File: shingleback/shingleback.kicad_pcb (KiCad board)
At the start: 2 copper layers, 117.8 x 86.2 mm, 45 parts

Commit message: final rev1 commit before manufacturing
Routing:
- net (no net): track 829.0 -> 841.0 mm

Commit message: shingleback rev2
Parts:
- removed the ? at (125.0, 83.5)
- removed the ? at (162.2, 30.7)
- removed the ? at (118.5, 88.0)
- removed the ? at (125.0, 88.0)
- removed the ? at (155.8, 30.7)
- removed the ? at (118.5, 83.5)
- removed the ? at (155.8, 26.2)
- removed the ? at (162.2, 26.2)
- removed the R at (131.8, 105.0)
- removed the R at (150.8, 67.0)
- removed the R at (93.8, 48.0)
- removed the R at (164.5, 108.2)
- removed the R at (150.8, 105.0)
- removed the R at (129.2, 57.8)
- removed the R at (131.8, 48.0)
- removed the R at (148.2, 67.0)
- removed the R at (150.8, 48.0)
- removed the R at (110.2, 67.0)
- removed the R at (129.2, 76.8)
- removed the R at (91.2, 86.0)
- removed the R at (91.2, 105.0)
- removed the R at (112.8, 38.8)
- removed the R at (110.2, 86.0)
- removed the R at (148.2, 86.0)
- removed the REF at (185.0, 62.0)
- removed the REF at (185.0, 88.2)
- removed the REF** at (161.5, 73.8)
- removed the REF** at (183.7, 100.8)
- removed the REF** at (176.1, 94.9)
- removed the S14 at (159.0, 62.1)
- removed the S14 at (140.0, 62.1)
- removed the S14 at (121.0, 71.8)
- removed the S14 at (140.0, 81.1)
- removed the S14 at (102.0, 81.1)
- removed the S14 at (121.0, 52.8)
- removed the S14 at (140.0, 100.1)
- removed the S14 at (121.0, 33.8)
- removed the S14 at (102.0, 43.1)
- removed the S14 at (140.0, 43.1)
- removed the S14 at (159.1, 100.1)
- removed the S14 at (83.0, 81.1)
- removed the S14 at (102.0, 62.1)
- removed the S14 at (159.0, 43.1)
- removed the S14 at (83.0, 100.1)
- added ?: , , F.Cu at (76.0, 101.0)
- added ?: , , F.Cu at (76.0, 105.5)
- added ?: , , F.Cu at (36.5, 58.0)
- added ?: , , F.Cu at (43.0, 58.0)
- added ?: , , F.Cu at (60.5, 105.5)
- added ?: , , F.Cu at (30.0, 73.9)
- added ?: , , F.Cu at (30.0, 79.0)
- added ?: , , F.Cu at (30.0, 76.5)
- added ?: , , F.Cu at (69.5, 105.5)
- added ?: , , F.Cu at (36.5, 53.5)
- added ?: , , F.Cu at (43.0, 53.5)
- added ?: , , F.Cu at (67.0, 101.0)
- added ?: , , F.Cu at (60.5, 101.0)
- added ?: , , F.Cu at (30.0, 81.5)
- added ?: , , F.Cu at (78.5, 105.5)
- added ?: , , F.Cu at (69.5, 101.0)
- added ?: , , F.Cu at (85.0, 105.5)
- added ?: , , F.Cu at (30.0, 84.1)
- added ?: , , F.Cu at (78.5, 101.0)
- added ?: , , F.Cu at (67.0, 105.5)
- added ?: , , F.Cu at (85.0, 101.0)
- added R: d, Diode_THT:D_DO-35_SOD27_P7.62mm_Horizontal, F.Cu at (46.5, 93.6)
- added R: d, Diode_THT:D_DO-35_SOD27_P7.62mm_Horizontal, F.Cu at (46.5, 74.6)
- added R: d, Diode_THT:D_DO-35_SOD27_P7.62mm_Horizontal, F.Cu at (107.0, 111.1)
- added R: d, Diode_THT:D_DO-35_SOD27_P7.62mm_Horizontal, F.Cu at (39.5, 101.0)
- added R: d, Diode_THT:D_DO-35_SOD27_P7.62mm_Horizontal, F.Cu at (50.0, 55.6)
- added R: d, Diode_THT:D_DO-35_SOD27_P7.62mm_Horizontal, F.Cu at (69.0, 74.6)
- added R: d, Diode_THT:D_DO-35_SOD27_P7.62mm_Horizontal, F.Cu at (88.0, 111.1)
- added R: d, Diode_THT:D_DO-35_SOD27_P7.62mm_Horizontal, F.Cu at (50.0, 93.6)
- added R: d, Diode_THT:D_DO-35_SOD27_P7.62mm_Horizontal, F.Cu at (69.0, 55.6)
- added R: d, Diode_THT:D_DO-35_SOD27_P7.62mm_Horizontal, F.Cu at (107.0, 55.6)
- added R: d, Diode_THT:D_DO-35_SOD27_P7.62mm_Horizontal, F.Cu at (49.5, 101.0)
- added R: d, Diode_THT:D_DO-35_SOD27_P7.62mm_Horizontal, F.Cu at (125.5, 92.5)
- added R: d, Diode_THT:D_DO-35_SOD27_P7.62mm_Horizontal, F.Cu at (88.0, 74.6)
- added R: d, Diode_THT:D_DO-35_SOD27_P7.62mm_Horizontal, F.Cu at (49.9, 74.6)
- added R: d, Diode_THT:D_DO-35_SOD27_P7.62mm_Horizontal, F.Cu at (69.0, 93.6)
- added R: d, Diode_THT:D_DO-35_SOD27_P7.62mm_Horizontal, F.Cu at (126.0, 111.1)
- added R: d, Diode_THT:D_DO-35_SOD27_P7.62mm_Horizontal, F.Cu at (88.0, 93.6)
- added R: d, Diode_THT:D_DO-35_SOD27_P7.62mm_Horizontal, F.Cu at (44.5, 101.0)
- added R: d, Diode_THT:D_DO-35_SOD27_P7.62mm_Horizontal, F.Cu at (107.0, 74.6)
- added R: d, Diode_THT:D_DO-35_SOD27_P7.62mm_Horizontal, F.Cu at (88.0, 55.6)
- added REF: RJ45_gnawman, Connector_RJ:RJ45_gnawman, F.Cu at (140.0, 74.0)
- added REF: RJ45_gnawman, Connector_RJ:RJ45_gnawman, B.Cu at (140.0, 98.0)
- added REF**: RotaryEncoder_gnawman, Rotary_Encoder:RotaryEncoder_gnawman, F.Cu at (118.0, 81.2)
- added S14: , MX, F.Cu at (95.8, 107.5)
- added S14: , MX, F.Cu at (114.8, 50.5)
- added S14: , MX, F.Cu at (95.8, 69.5)
- added S14: , MX, F.Cu at (114.8, 107.5)
- added S14: , MX, F.Cu at (38.8, 88.5)
- added S14: , MX, F.Cu at (76.8, 88.5)
- added S14: , MX, F.Cu at (95.8, 50.5)
- added S14: , MX, F.Cu at (57.8, 88.5)
- added S14: , MX, F.Cu at (95.8, 88.5)
- added S14: , MX, F.Cu at (114.8, 69.5)
- added S14: , MX, F.Cu at (76.8, 50.5)
- added S14: , MX, F.Cu at (133.8, 107.5)
- added S14: , MX, F.Cu at (76.8, 69.5)
- added S14: , MX, F.Cu at (57.8, 50.5)
- added S14: , MX, F.Cu at (38.8, 69.5)
- added S14: , MX, F.Cu at (57.8, 69.5)
- moved MCU1 46.4 mm to (133.6, 59.0)
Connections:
- MCU1 pad 1: (no net) -> rot1
- MCU1 pad 10: col6 -> row3
- MCU1 pad 11: col7 -> row4
- MCU1 pad 12: col8 -> row5
- MCU1 pad 13: (no net) -> RAW
- MCU1 pad 14: GND -> (no net)
- MCU1 pad 15: (no net) -> RST
- MCU1 pad 17: (no net) -> col8
- MCU1 pad 18: (no net) -> col7
- MCU1 pad 19: (no net) -> col6
- MCU1 pad 2: (no net) -> rot2
- MCU1 pad 20: (no net) -> col5
- MCU1 pad 21: row1 -> col4
- MCU1 pad 22: row2 -> col3
- MCU1 pad 23: row3 -> col2
- MCU1 pad 24: row4 -> col1
- MCU1 pad 4: GND -> (no net)
- MCU1 pad 5: col1 -> row1
- MCU1 pad 6: col2 -> exp3
- MCU1 pad 7: col3 -> exp2
- MCU1 pad 8: col4 -> exp1
- MCU1 pad 9: col5 -> row2
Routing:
- net (no net): track 841.0 -> 306.1 mm
- net RST: track 0.00 -> 118.7 mm
- net exp1: track 0.00 -> 114.0 mm
- net col4: track 110.7 -> 224.5 mm
- net exp2: track 0.00 -> 110.9 mm
- net exp3: track 0.00 -> 109.9 mm
- net row5: track 0.00 -> 105.8 mm
- net col1: track 246.3 -> 160.9 mm
- net VCC: track 79.5 -> 146.3 mm
- net row1: track 180.5 -> 117.8 mm, vias 1 -> 0
- net row2: track 177.7 -> 120.7 mm, vias 1 -> 0
- net col3: track 165.6 -> 222.4 mm
- net row4: track 139.9 -> 95.8 mm
- net rot1: track 0.00 -> 41.6 mm
- net rot2: track 0.00 -> 37.0 mm
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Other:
- board size 117.8 x 86.2 mm -> 119.5 x 76 mm
- board text added: "EX1"
- board text added: "EX2"
- board text added: "EX3"
- board text added: "GND"
- board text added: "VCC"
- board text added: "shingleback rev2"
- board text removed: "button"
- board text removed: "empty"
- board text removed: "joy"
- board text removed: "rj45"
- board text removed: "shingleback rev1"
- board text removed: "stick"
- board text removed: "switch"
- board text removed: "this space intentionally left blank"

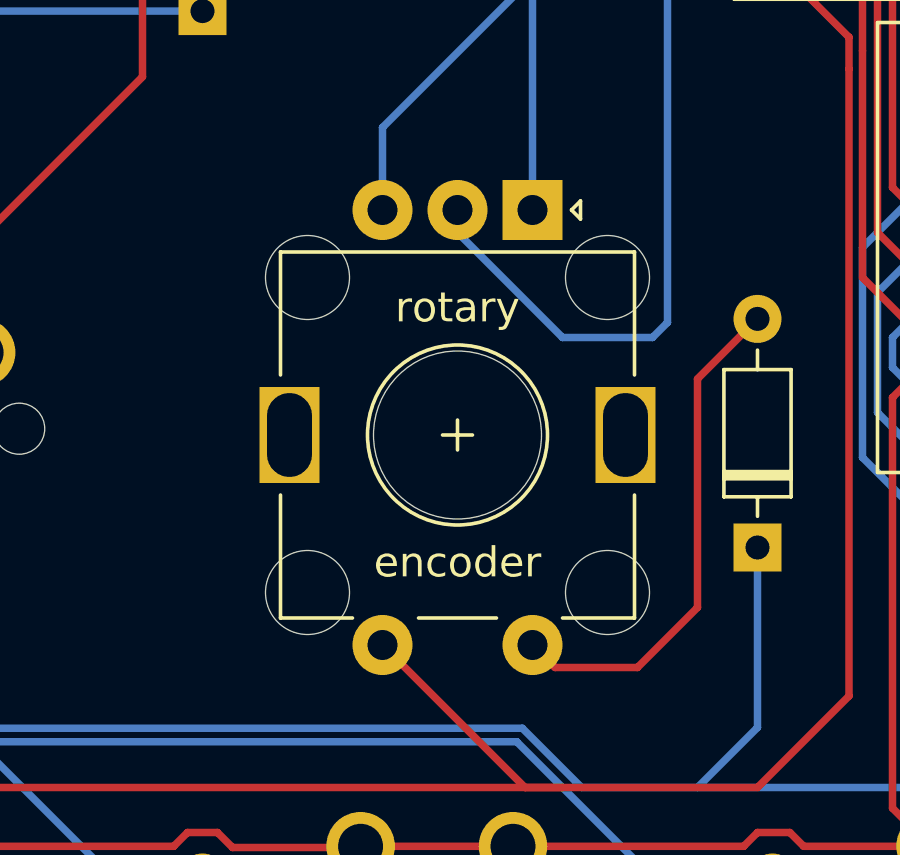
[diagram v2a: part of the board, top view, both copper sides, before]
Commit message: changed net names to reflect reality
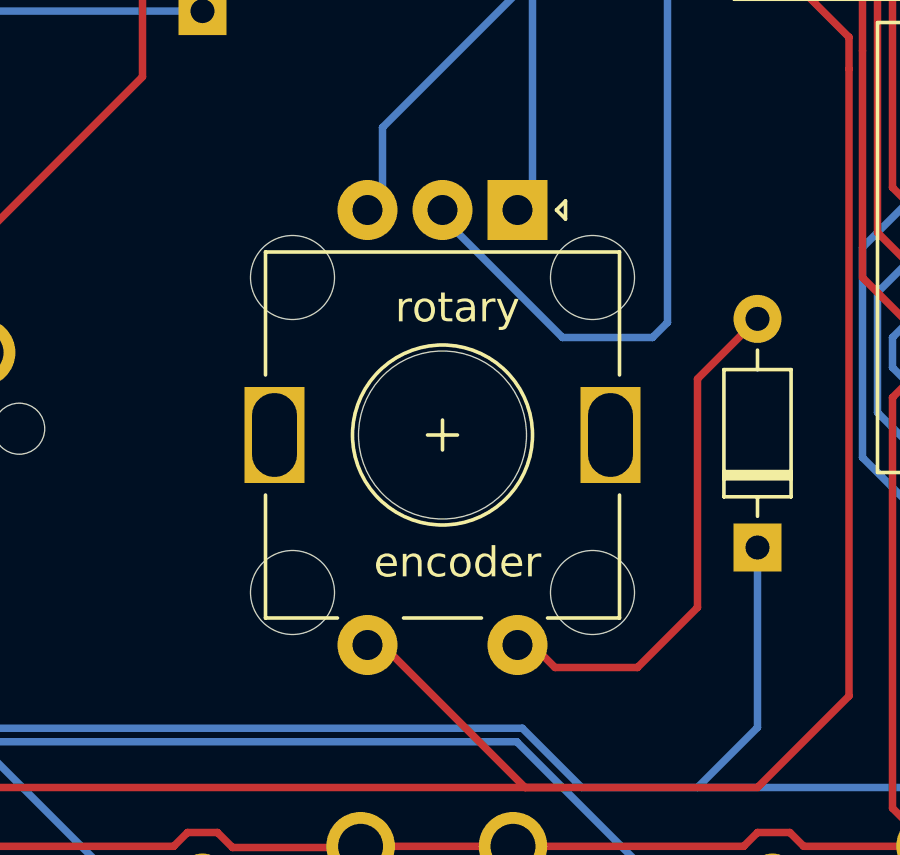
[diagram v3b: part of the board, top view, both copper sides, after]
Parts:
- moved REF** 0.50 mm to (117.5, 81.2)
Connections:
- ? pad 2: row5 -> row4 (x6)
- MCU1 pad 10: row3 -> row2
- MCU1 pad 11: row4 -> row3
- MCU1 pad 12: row5 -> row4
- MCU1 pad 17: col8 -> col4
- MCU1 pad 18: col7 -> col5
- MCU1 pad 20: col5 -> col7
- MCU1 pad 21: col4 -> col0
- MCU1 pad 22: col3 -> col1
- MCU1 pad 24: col1 -> col3
- MCU1 pad 5: row1 -> row0
- MCU1 pad 9: row2 -> row1
- R pad 1: col4 -> col0 (x5)
- R pad 1: col3 -> col1 (x5)
- R pad 1: col1 -> col3 (x5)
- REF pad : col5 -> col7
- REF pad : col3 -> col1
- REF** pad S1: row5 -> row4
- S14 pad 1: row4 -> row3 (x4)
- S14 pad 1: row1 -> row0 (x4)
- S14 pad 1: row2 -> row1 (x4)
- S14 pad 1: row3 -> row2 (x4)
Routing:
- net col0: track 0.00 -> 224.5 mm
- net col4: track 224.5 -> 26.8 mm
- net row0: track 0.00 -> 117.8 mm
- net row5: track 105.8 -> 0.00 mm
- net col3: track 222.4 -> 160.9 mm
- net col1: track 160.9 -> 222.4 mm
- net row3: track 130.8 -> 95.8 mm
- net col8: track 26.8 -> 0.00 mm
- net row2: track 120.7 -> 130.8 mm
- net row4: track 95.8 -> 105.8 mm
- net row1: track 117.8 -> 120.7 mm
- net col7: track 26.7 -> 28.7 mm
- net col5: track 28.7 -> 26.7 mm

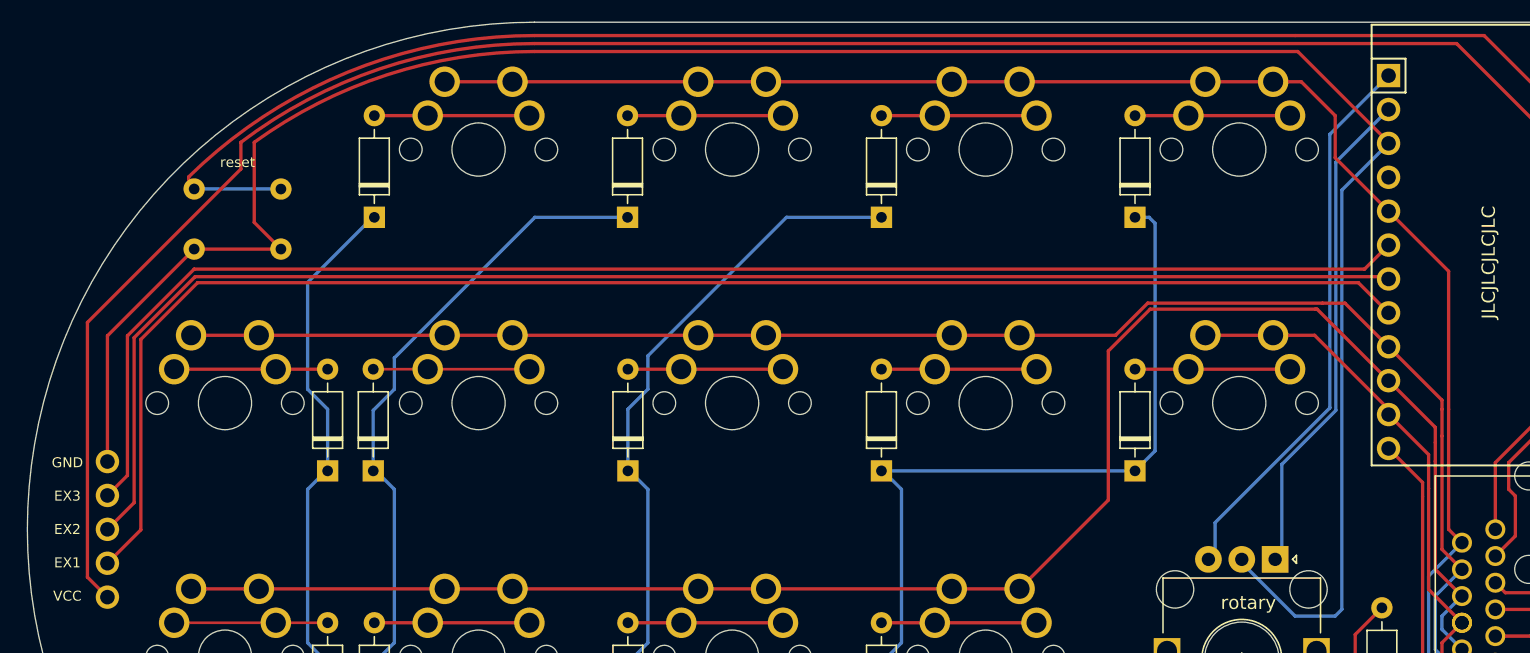
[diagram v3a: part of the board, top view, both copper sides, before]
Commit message: ensuring expansion slot can be used for I2C communication
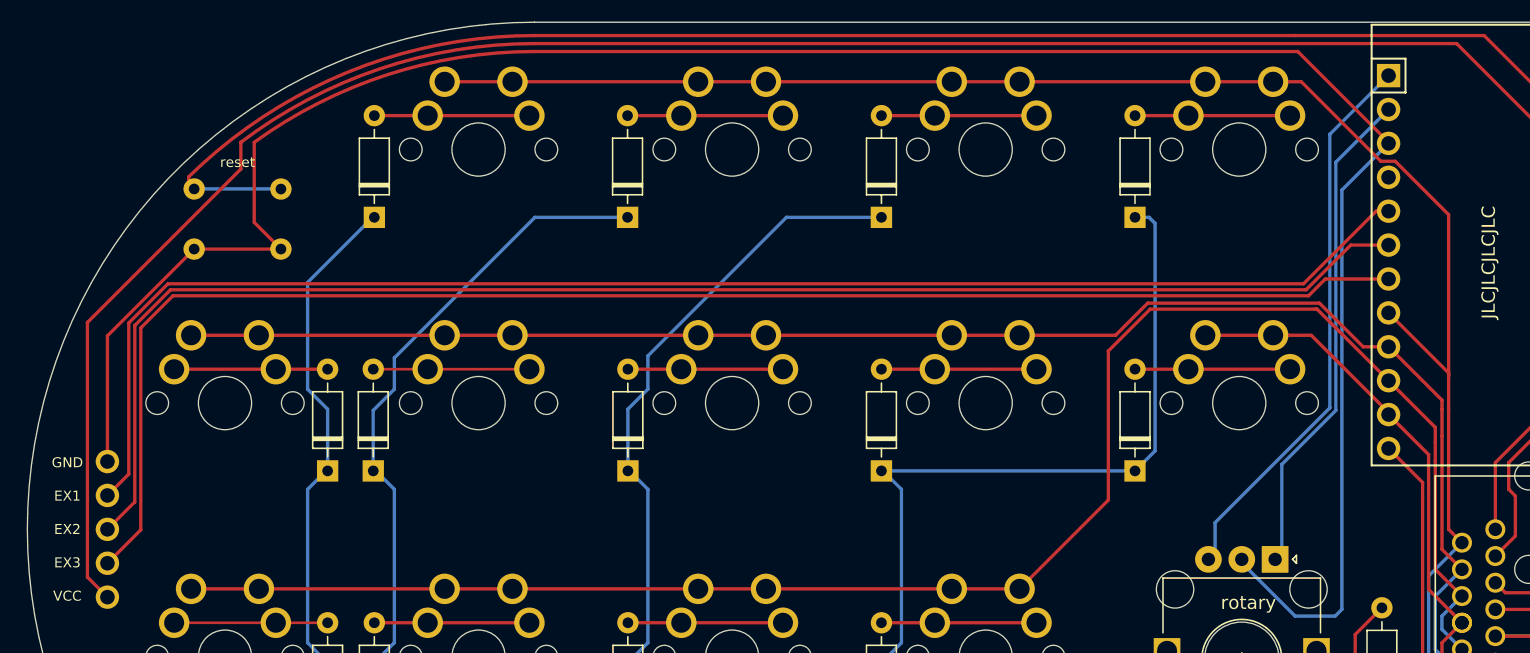
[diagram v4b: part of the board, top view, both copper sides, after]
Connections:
- ? pad : exp3 -> exp1
- ? pad : exp1 -> exp3
- MCU1 pad 5: row0 -> exp1
- MCU1 pad 6: exp3 -> exp2
- MCU1 pad 7: exp2 -> exp3
- MCU1 pad 8: exp1 -> row0
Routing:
- net row0: track 117.8 -> 125.0 mm
- net exp3: track 109.9 -> 113.7 mm
- net exp1: track 114.0 -> 111.5 mm
- net exp2: track 110.9 -> 112.6 mm
